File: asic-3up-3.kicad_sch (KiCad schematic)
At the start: 79 parts, among them J10 Conn_01x01, J11 Conn_01x01, U4 SN74AVC4T774, U5 25MHz, U66 MCP1824T-1202E/OT, U67 MCP1824T-1202E/OT, U68 MCP1824T-1202E/OT, U69 MCP1824T-0802E, U70 MCP1824T-0802E, U71 MCP1824T-0802E, U72 BM1362AC_MODE1, U73 BM1362AC_MODE0, U74 BM1362AC_MODE1

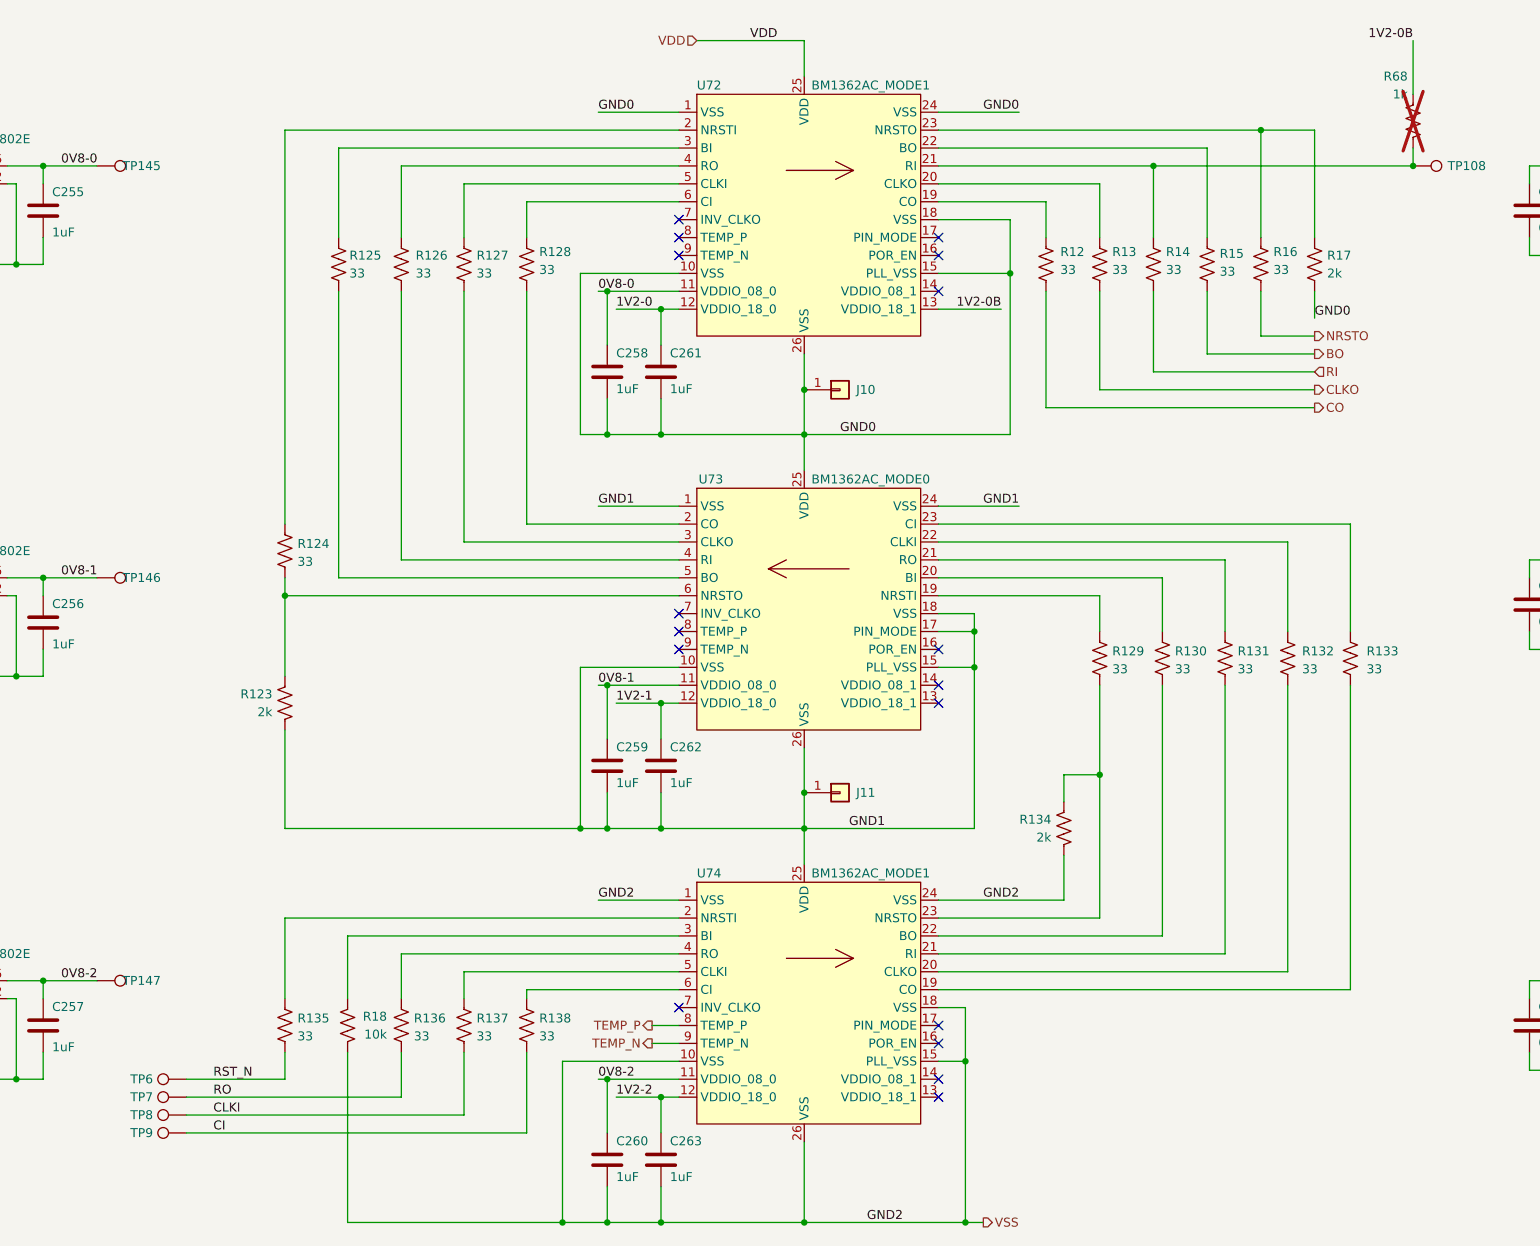
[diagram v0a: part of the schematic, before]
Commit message: added topside data test pads. cleaned up power pads some more.
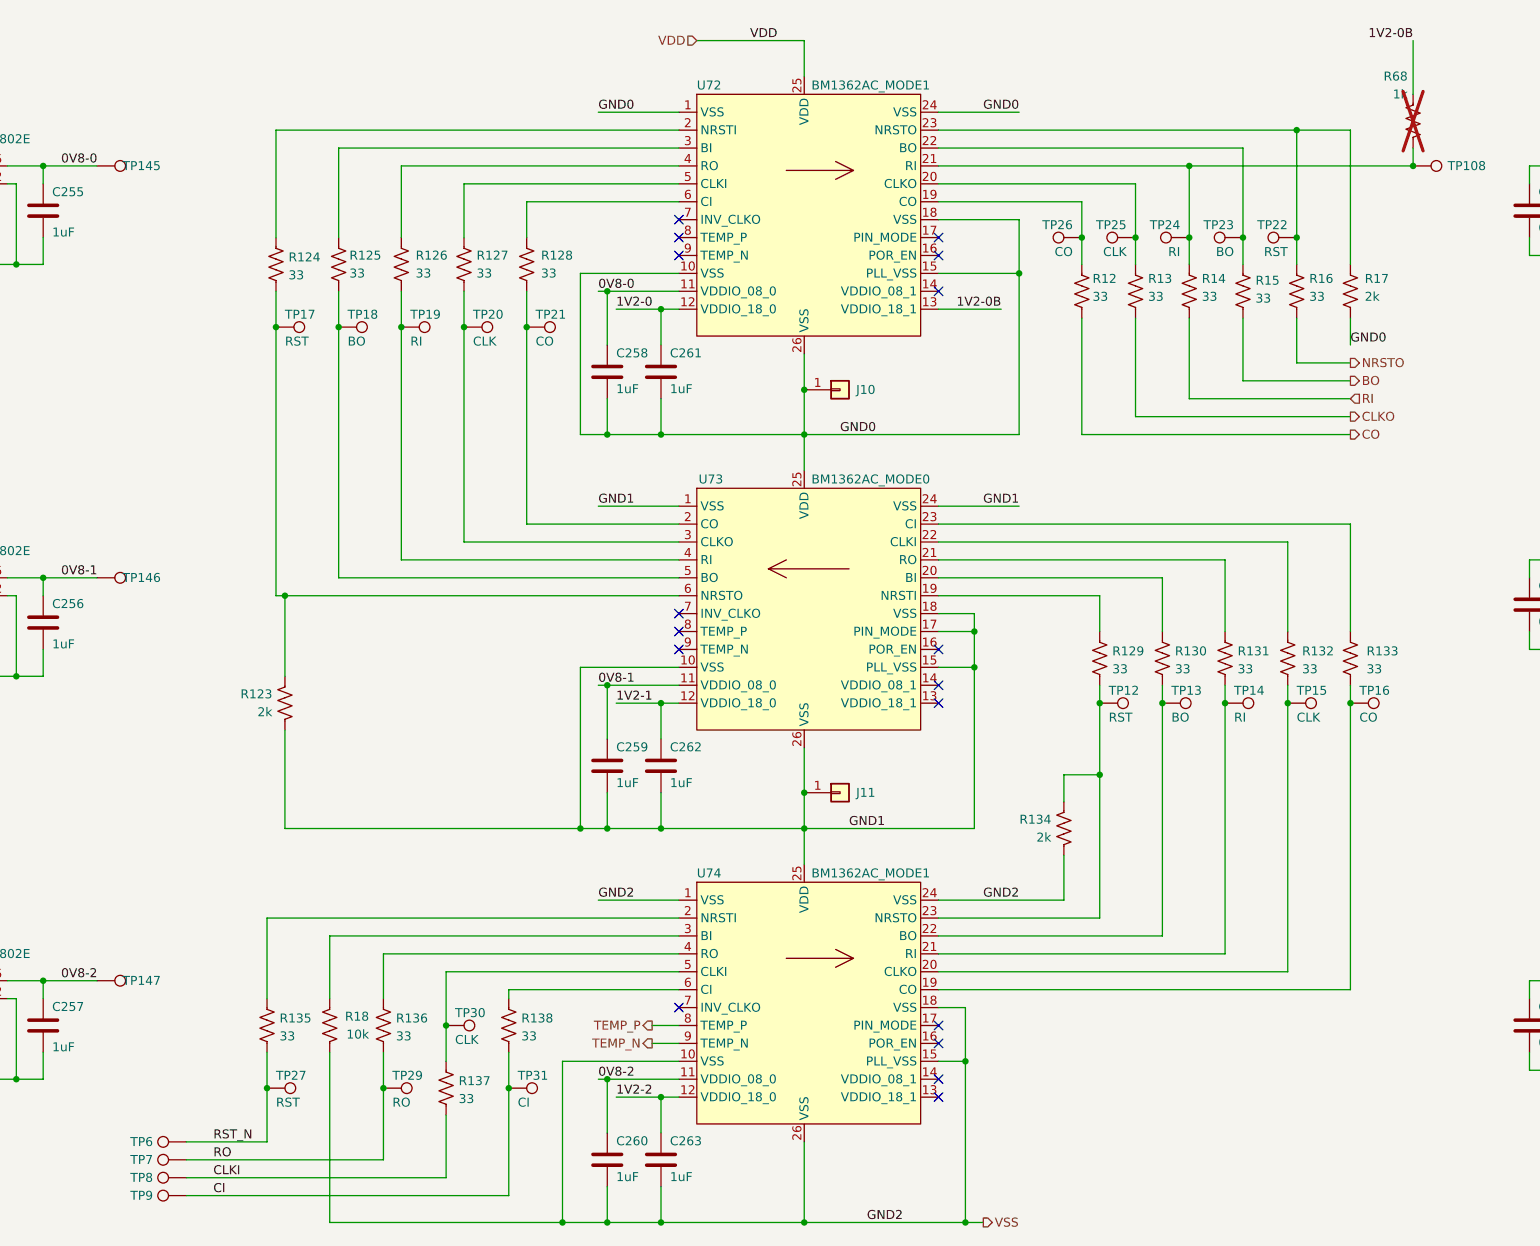
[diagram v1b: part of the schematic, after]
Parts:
- added TP12, TP17, TP22, TP27: RST, emberone:TestPoint_Pad_1.0x0.4mm, symbol Connector:TestPoint
- added TP13, TP18, TP23: BO, emberone:TestPoint_Pad_1.0x0.4mm, symbol Connector:TestPoint
- added TP14, TP19, TP24: RI, emberone:TestPoint_Pad_1.0x0.4mm, symbol Connector:TestPoint
- added TP15, TP20, TP25, TP30: CLK, emberone:TestPoint_Pad_1.0x0.4mm, symbol Connector:TestPoint
- added TP16, TP21, TP26: CO, emberone:TestPoint_Pad_1.0x0.4mm, symbol Connector:TestPoint
- added TP29: RO, emberone:TestPoint_Pad_1.0x0.4mm, symbol Connector:TestPoint
- added TP31: CI, emberone:TestPoint_Pad_1.0x0.4mm, symbol Connector:TestPoint
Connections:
- net CI: now also TP31.1
- net RO: now also TP29.1
- net RST_N: now also TP27.1
- net at R130.2, U74.22 (BO): now also TP13.1
- net at R133.2, U74.19 (CO): now also TP16.1
- net at R128.2, U73.2 (CO): now also TP21.1
- net at R12.1, U72.19 (CO): now also TP26.1
- net at R13.1, U72.20 (CLKO): now also TP25.1
- net at R14.1, R68.2, TP108.1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: now also TP24.1
- net at R15.1, U72.22 (BO): now also TP23.1
- net at R16.1, R17.1, U72.23 (NRSTO): now also TP22.1
- net at R129.2, R134.1, U74.23 (NRSTO): now also TP12.1
- net at R137.1, U74.5 (CLKI): now also TP30.1
- net at R127.2, U73.3 (CLKO): now also TP20.1
- net at R126.2, U73.4 (RI): now also TP19.1
- net at R125.2, U73.5 (BO): now also TP18.1
- net at R123.1, R124.2, U73.6 (NRSTO): now also TP17.1
- net at R132.2, U74.20 (CLKO): now also TP15.1
- net at R131.2, U74.21 (RI): now also TP14.1
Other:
- moved on the sheet: R12, R124, R13, R135, R136, R137, R138, R14, R15, R16, R17, R18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

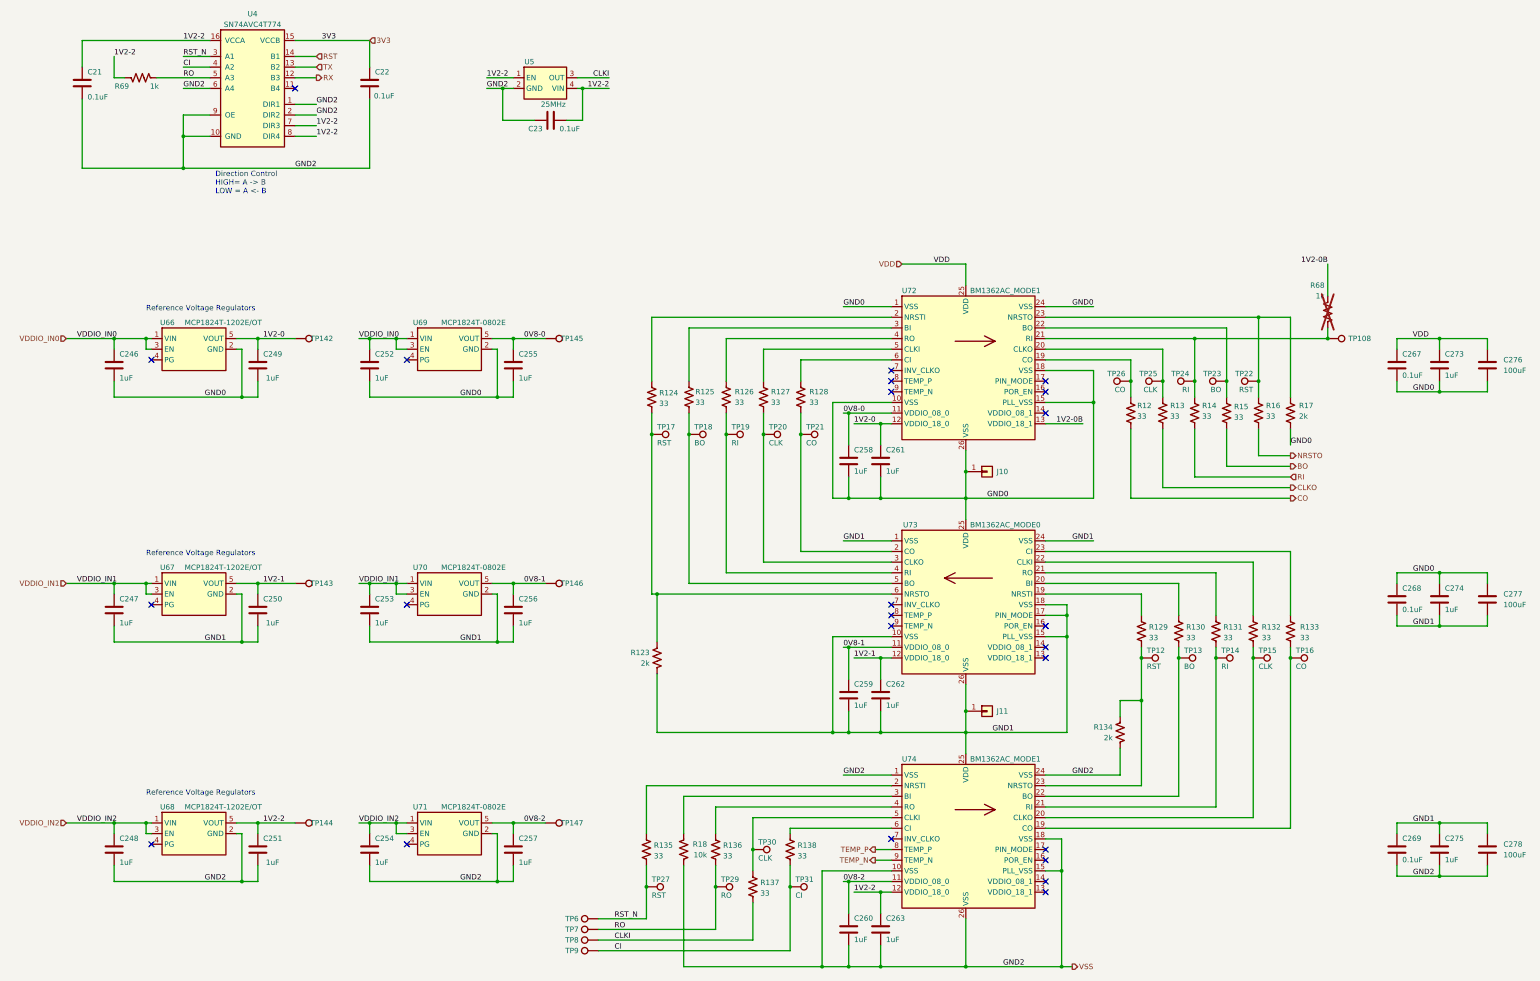
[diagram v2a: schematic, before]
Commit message: switch schematic to TPS546D24S regulator. get pcb mostly synced
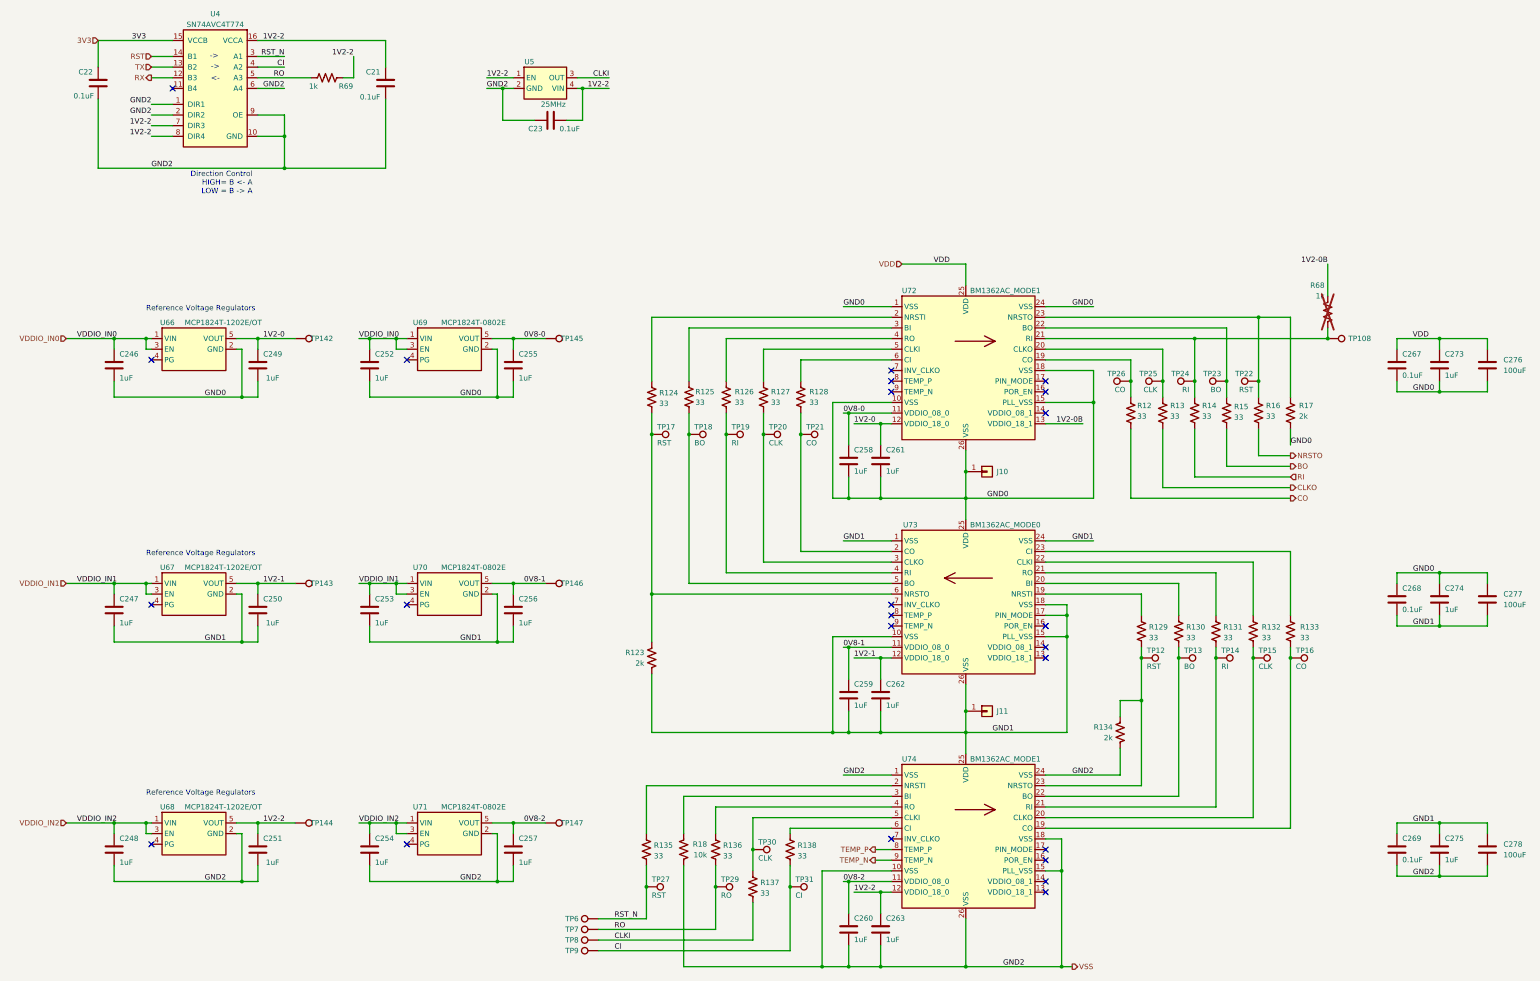
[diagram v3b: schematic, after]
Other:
- note added: "->"
- note added: "<-"
- note added: "Direction Control HIGH= B <- A LOW = B -> A"
- note removed: "Direction Control HIGH= A -> B LOW = A <- B"
- moved on the sheet: C21, C22, R69, U4

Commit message: add BOM, iBOM and position files
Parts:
- J10, J11: now left out of the parts list
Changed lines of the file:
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@@
 		(unit 1)
 		(exclude_from_sim no)
-		(in_bom yes)
+		(in_bom no)
 		(on_board yes)
 		(dnp no)
@@
 		(unit 1)
 		(exclude_from_sim no)
-		(in_bom yes)
+		(in_bom no)
 		(on_board yes)
 		(dnp no)

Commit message: corrected the voltage regulator input and output capacitors. Updated BOM, iBOM, cpos, gerbers and render.
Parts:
- U5: DK (none) -> 5852-SX3M25.000E20F30THNTR-ND
- U72, U73, U74: PARTNO (none) -> BM1362AC
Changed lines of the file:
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@@
 			)
 		)
-		(property "DK" ""
+		(property "DK" "5852-SX3M25.000E20F30THNTR-ND"
 			(at 160.02 44.45 0)
 			(effects
@@
 			)
 		)
+		(property "PARTNO" "BM1362AC"
+			(at 260.35 111.76 0)
+			(effects
+				(font
+					(size 1.27 1.27)
+				)
+				(hide yes)
+			)
+		)
 		(pin "12"
 		)
@@
 			)
 		)
+		(property "PARTNO" "BM1362AC"
+			(at 260.35 167.64 0)
+			(effects
+				(font
+					(size 1.27 1.27)
+				)
+				(hide yes)
+			)
+		)
 		(pin "10"
 		)
@@
 			(at 260.35 223.52 0)
 			(effects
+				(font
+					(size 1.27 1.27)
+				)
+				(hide yes)
+			)
+		)
+		(property "PARTNO" "BM1362AC"
+			(at 260.35 223.52 0)
+			(effects

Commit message: bump version to v6
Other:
- company: (none) -> 256Foundation
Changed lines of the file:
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@@
 	(title_block
 		(title "emberOne/00")
-		(date "2025-09-17")
-		(rev "5")
+		(date "2026-02-17")
+		(rev "v6")
+		(company "256Foundation")
+		(comment 1 "OHL-S-2.0")
 	)
 	(text "Reference Voltage Regulators"
